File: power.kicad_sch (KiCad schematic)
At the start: 60 parts, among them J19 Conn_Coaxial, Q1 CSD18511Q5A, Q2 CSD18511Q5A, Q3 CSD18511Q5A, Q4 CSD18511Q5A, U1 LM25119PSQ/NOPB, U2 DS4432U+, U3 INA260

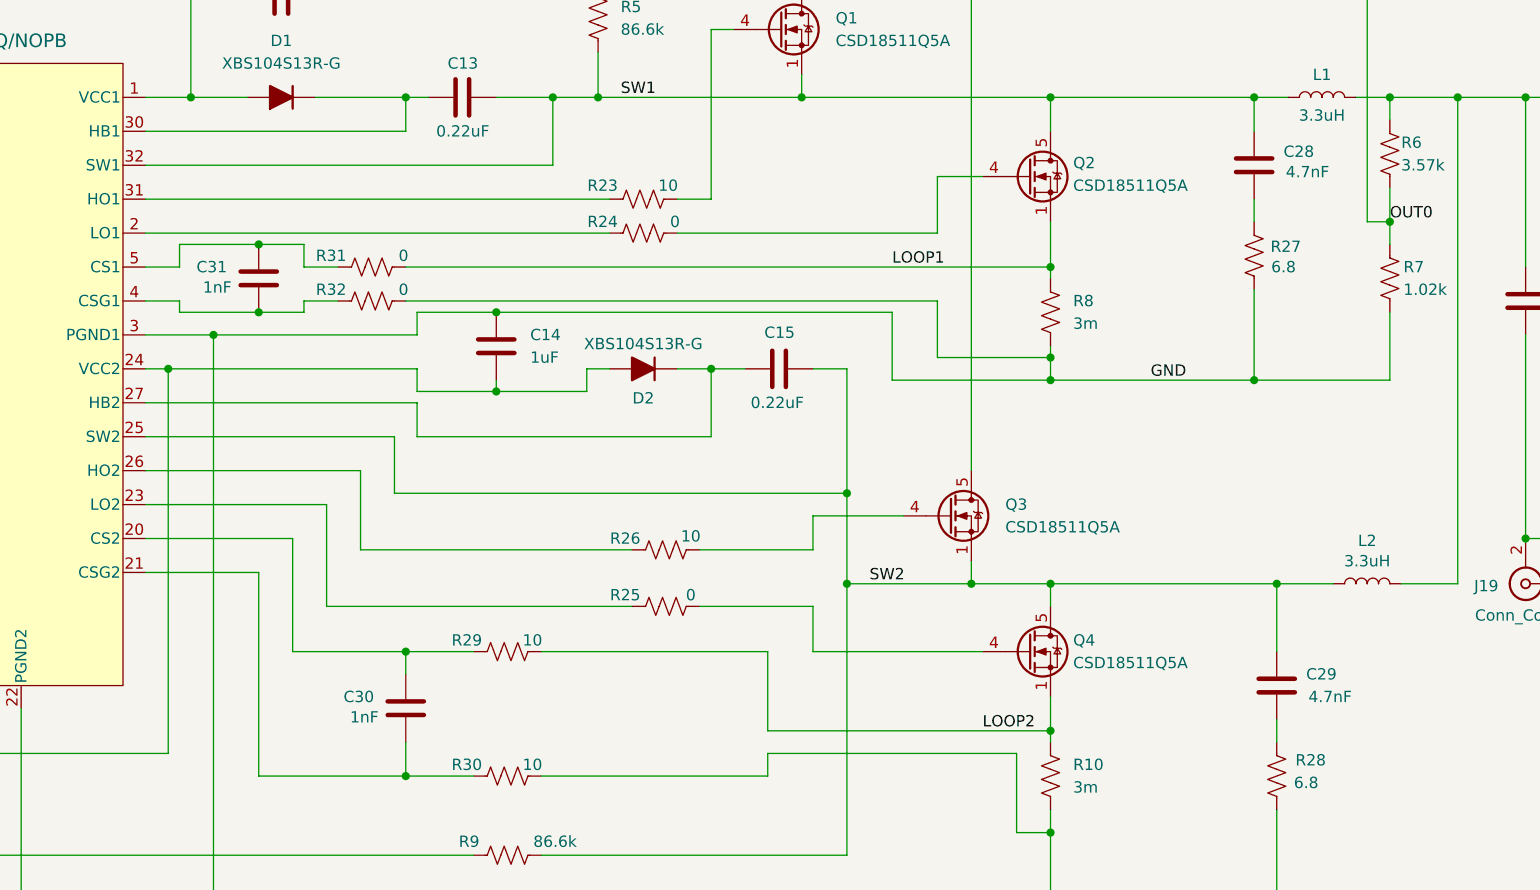
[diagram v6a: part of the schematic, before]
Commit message: reduced center pad paste amount. cleaned up ASIC footprint vias. moved vreg passives around to better fit model name
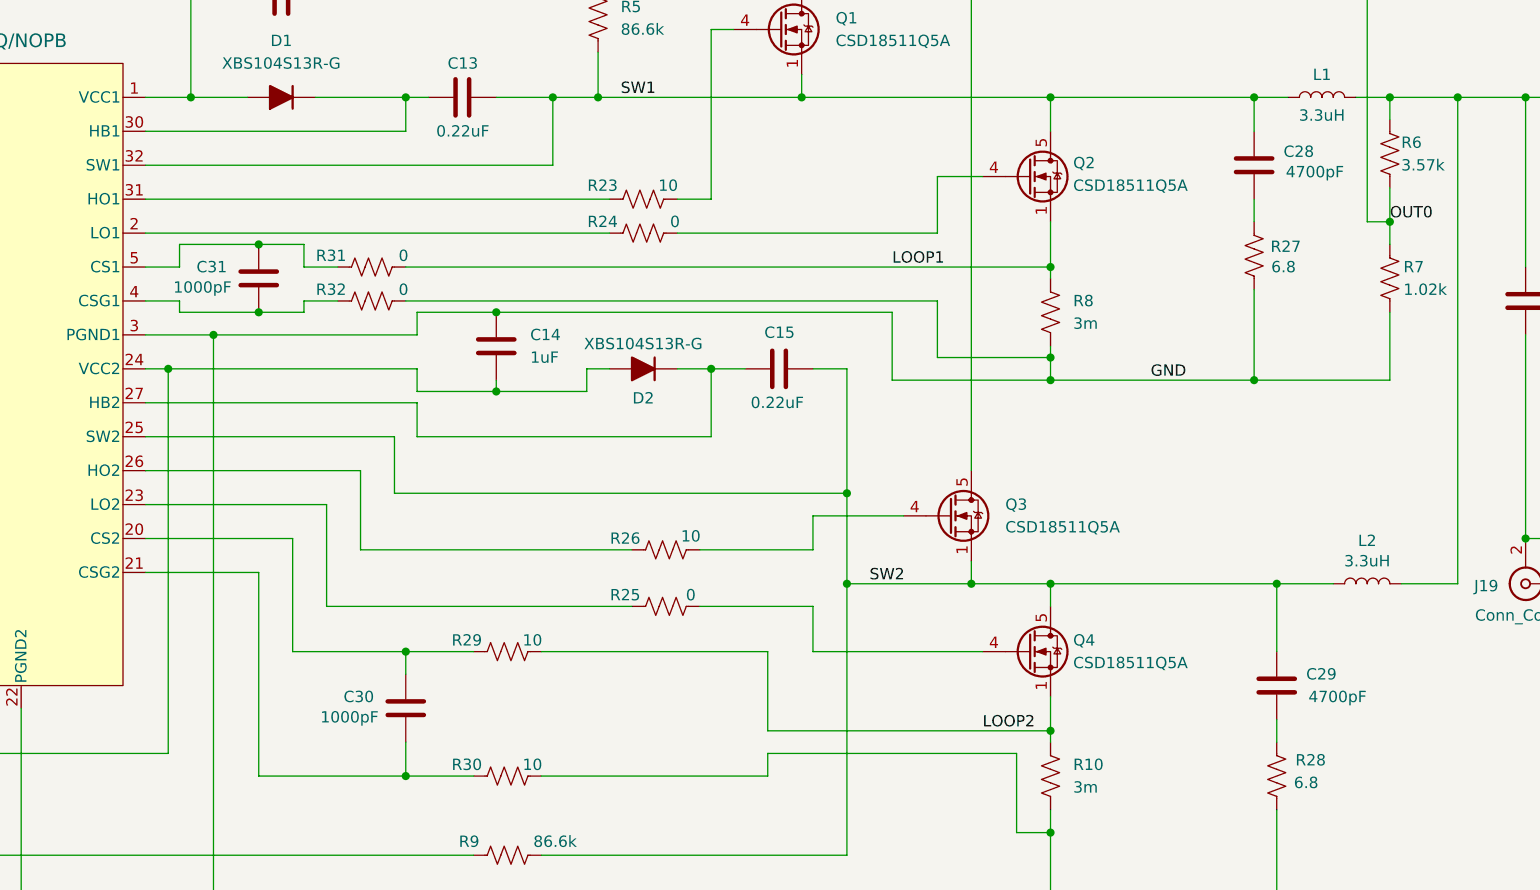
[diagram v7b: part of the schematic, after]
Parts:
- C26: DK (none) -> 1276-6470-1-ND; PARTNO (none) -> CL21B105KBFNNNG
- C27: DK (none) -> 311-1140-1-ND; PARTNO (none) -> CC0805KRX7R9BB104
- C28, C29: value 4.7nF -> 4700pF; DK (none) -> 311-1133-1-ND; PARTNO (none) -> CC0805KRX7R9BB472
- C30, C31: value 1nF -> 1000pF; DK (none) -> 1276-1169-1-ND; PARTNO (none) -> CL21B102KCANNNC
- R11: DK (none) -> 311-39.0KLRCT-ND; PARTNO (none) -> RC0402FR-0739KL
- R23, R26, R29, R30: DK (none) -> 311-10.0HRCT-ND; PARTNO (none) -> RC0603FR-0710RL
- R24, R25, R31, R32, R33: DK (none) -> 311-0.0HRCT-ND; PARTNO (none) -> RC0603FR-070RL
- R27, R28: DK (none) -> 13-RC0603FR-076R8LCT-ND; PARTNO (none) -> RC0603FR-076R8L
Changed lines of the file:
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@@
 			)
 		)
-		(property "DK" ""
+		(property "DK" "311-1140-1-ND"
 			(at 344.17 95.25 0)
 			(effects
@@
 			)
 		)
-		(property "PARTNO" ""
+		(property "PARTNO" "CC0805KRX7R9BB104"
 			(at 344.17 95.25 0)
 			(effects
@@
 			)
 		)
+		(property "DK" "311-10.0HRCT-ND"
+			(at 229.87 134.62 0)
+			(effects
+				(font
+					(size 1.27 1.27)
+				)
+				(hide yes)
+			)
+		)
+		(property "PARTNO" "RC0603FR-0710RL"
+			(at 229.87 134.62 0)
+			(effects
+				(font
+					(size 1.27 1.27)
+				)
+				(hide yes)
+			)
+		)
 		(pin "1"
 		)
@@
 			)
 		)
+		(property "DK" "311-0.0HRCT-ND"
+			(at 214.63 91.44 0)
+			(effects
+				(font
+					(size 1.27 1.27)
+				)
+				(hide yes)
+			)
+		)
+		(property "PARTNO" "RC0603FR-070RL"
+			(at 214.63 91.44 0)
+			(effects
+				(font
+					(size 1.27 1.27)
+				)
+				(hide yes)
+			)
+		)
 		(pin "1"
 		)
@@
 			)
 		)
-		(property "DK" ""
+		(property "DK" "13-RC0603FR-076R8LCT-ND"
 			(at 316.23 148.59 0)
 			(effects
@@
 			)
 		)
-		(property "PARTNO" ""
+		(property "PARTNO" "RC0603FR-076R8L"
 			(at 316.23 148.59 0)
 			(effects
@@
 			)
 		)
+		(property "DK" "311-10.0HRCT-ND"
+			(at 245.11 83.82 0)
+			(effects
+				(font
+					(size 1.27 1.27)
+				)
+				(hide yes)
+			)
+		)
+		(property "PARTNO" "RC0603FR-0710RL"
+			(at 245.11 83.82 0)
+			(effects
+				(font
+					(size 1.27 1.27)
+				)
+				(hide yes)
+			)
+		)
 		(pin "1"
 		)
@@
 			)
 		)
-		(property "Value" "4.7nF"
+		(property "Value" "4700pF"
 			(at 317.246 80.772 0)
 			(effects
@@
 			)
 		)
-		(property "DK" ""
+		(property "DK" "311-1133-1-ND"
 			(at 313.69 80.01 0)
 			(effects
@@
 			)
 		)
-		(property "PARTNO" ""
+		(property "PARTNO" "CC0805KRX7R9BB472"
 			(at 313.69 80.01 0)
 			(effects
@@
 			)
 		)
+		(property "DK" "311-10.0HRCT-ND"
+			(at 247.65 123.19 0)
+			(effects
+				(font
+					(size 1.27 1.27)
+				)
+				(hide yes)
+			)
+		)
+		(property "PARTNO" "RC0603FR-0710RL"
+			(at 247.65 123.19 0)
+			(effects
+				(font
+					(size 1.27 1.27)
+				)
+				(hide yes)
+			)
+		)
 		(pin "1"
 		)
@@
 			)
 		)
-		(property "DK" ""
+		(property "DK" "13-RC0603FR-076R8LCT-ND"
 			(at 313.69 90.17 0)
 			(effects
@@
 			)
 		)
-		(property "PARTNO" ""
+		(property "PARTNO" "RC0603FR-076R8L"
 			(at 313.69 90.17 0)
 			(effects
@@
 			)
 		)
+		(property "DK" "311-0.0HRCT-ND"
+			(at 247.65 129.54 0)
+			(effects
+				(font
+					(size 1.27 1.27)
+				)
+				(hide yes)
+			)
+		)
+		(property "PARTNO" "RC0603FR-070RL"
+			(at 247.65 129.54 0)
+			(effects
+				(font
+					(size 1.27 1.27)
+				)
+				(hide yes)
+			)
+		)
 		(pin "1"
 		)
@@
 			)
 		)
+		(property "DK" "311-0.0HRCT-ND"
+			(at 214.63 95.25 0)
+			(effects
+				(font
+					(size 1.27 1.27)
+				)
+				(hide yes)
+			)
+		)
+		(property "PARTNO" "RC0603FR-070RL"
+			(at 214.63 95.25 0)
+			(effects
+				(font
+					(size 1.27 1.27)
+				)
+				(hide yes)
+			)
+		)
 		(pin "1"
 		)
@@
 			)
 		)
-		(property "Value" "1nF"
+		(property "Value" "1000pF"
 			(at 215.392 141.986 0)
 			(effects
@@
 			)
 		)
-		(property "DK" ""
+		(property "DK" "1276-1169-1-ND"
 			(at 218.44 140.97 0)
 			(effects
@@
 			)
 		)
-		(property "PARTNO" ""
+		(property "PARTNO" "CL21B102KCANNNC"
 			(at 218.44 140.97 0)
 			(effects
@@
 			)
 		)
+		(property "DK" "311-0.0HRCT-ND"
+			(at 245.11 87.63 0)
+			(effects
+				(font
+					(size 1.27 1.27)
+				)
+				(hide yes)
+			)
+		)
+		(property "PARTNO" "RC0603FR-070RL"
+			(at 245.11 87.63 0)
+			(effects
+				(font
+					(size 1.27 1.27)
+				)
+				(hide yes)
+			)
+		)
 		(pin "1"
 		)
@@
 			)
 		)
-		(property "Value" "1nF"
+		(property "Value" "1000pF"
 			(at 198.882 93.726 0)
 			(effects
@@
 			)
 		)
-		(property "DK" ""
+		(property "DK" "1276-1169-1-ND"
 			(at 201.93 92.71 0)
 			(effects
@@
 			)
 		)
-		(property "PARTNO" ""
+		(property "PARTNO" "CL21B102KCANNNC"
 			(at 201.93 92.71 0)
 			(effects
@@
 			)
 		)
+		(property "DK" "311-10.0HRCT-ND"
+			(at 229.87 148.59 0)
+			(effects
+				(font
+					(size 1.27 1.27)
+				)
+				(hide yes)
+			)
+		)
+		(property "PARTNO" "RC0603FR-0710RL"
+			(at 229.87 148.59 0)
+			(effects
+				(font
+					(size 1.27 1.27)
+				)
+				(hide yes)
+			)
+		)
 		(pin "1"
 		)
@@
 			)
 		)
-		(property "Value" "4.7nF"
+		(property "Value" "4700pF"
 			(at 319.786 139.7 0)
 			(effects
@@
 			)
 		)
-		(property "DK" ""
+		(property "DK" "311-1133-1-ND"
 			(at 316.23 138.43 0)
 			(effects
@@
 			)
 		)
-		(property "PARTNO" ""
+		(property "PARTNO" "CC0805KRX7R9BB472"
 			(at 316.23 138.43 0)
 			(effects
@@
 			)
 		)
+		(property "DK" "311-0.0HRCT-ND"
+			(at 77.47 78.74 0)
+			(effects
+				(font
+					(size 1.27 1.27)
+				)
+				(hide yes)
+			)
+		)
+		(property "PARTNO" "RC0603FR-070RL"
+			(at 77.47 78.74 0)
+			(effects
+				(font
+					(size 1.27 1.27)
+				)
+				(hide yes)
+			)
+		)
 		(pin "1"
 		)
@@
 			)
 		)
-		(property "DK" ""
+		(property "DK" "1276-6470-1-ND"
 			(at 355.6 95.25 0)
 			(effects
@@
 			)
 		)
-		(property "PARTNO" ""
+		(property "PARTNO" "CL21B105KBFNNNG"
 			(at 355.6 95.25 0)
 			(effects
@@
 			)
 		)
-		(property "DK" ""
+		(property "DK" "311-39.0KLRCT-ND"
 			(at 295.91 219.71 0)
 			(effects
@@
 			)
 		)
-		(property "PARTNO" ""
+		(property "PARTNO" "RC0402FR-0739KL"
 			(at 295.91 219.71 0)
 			(effects

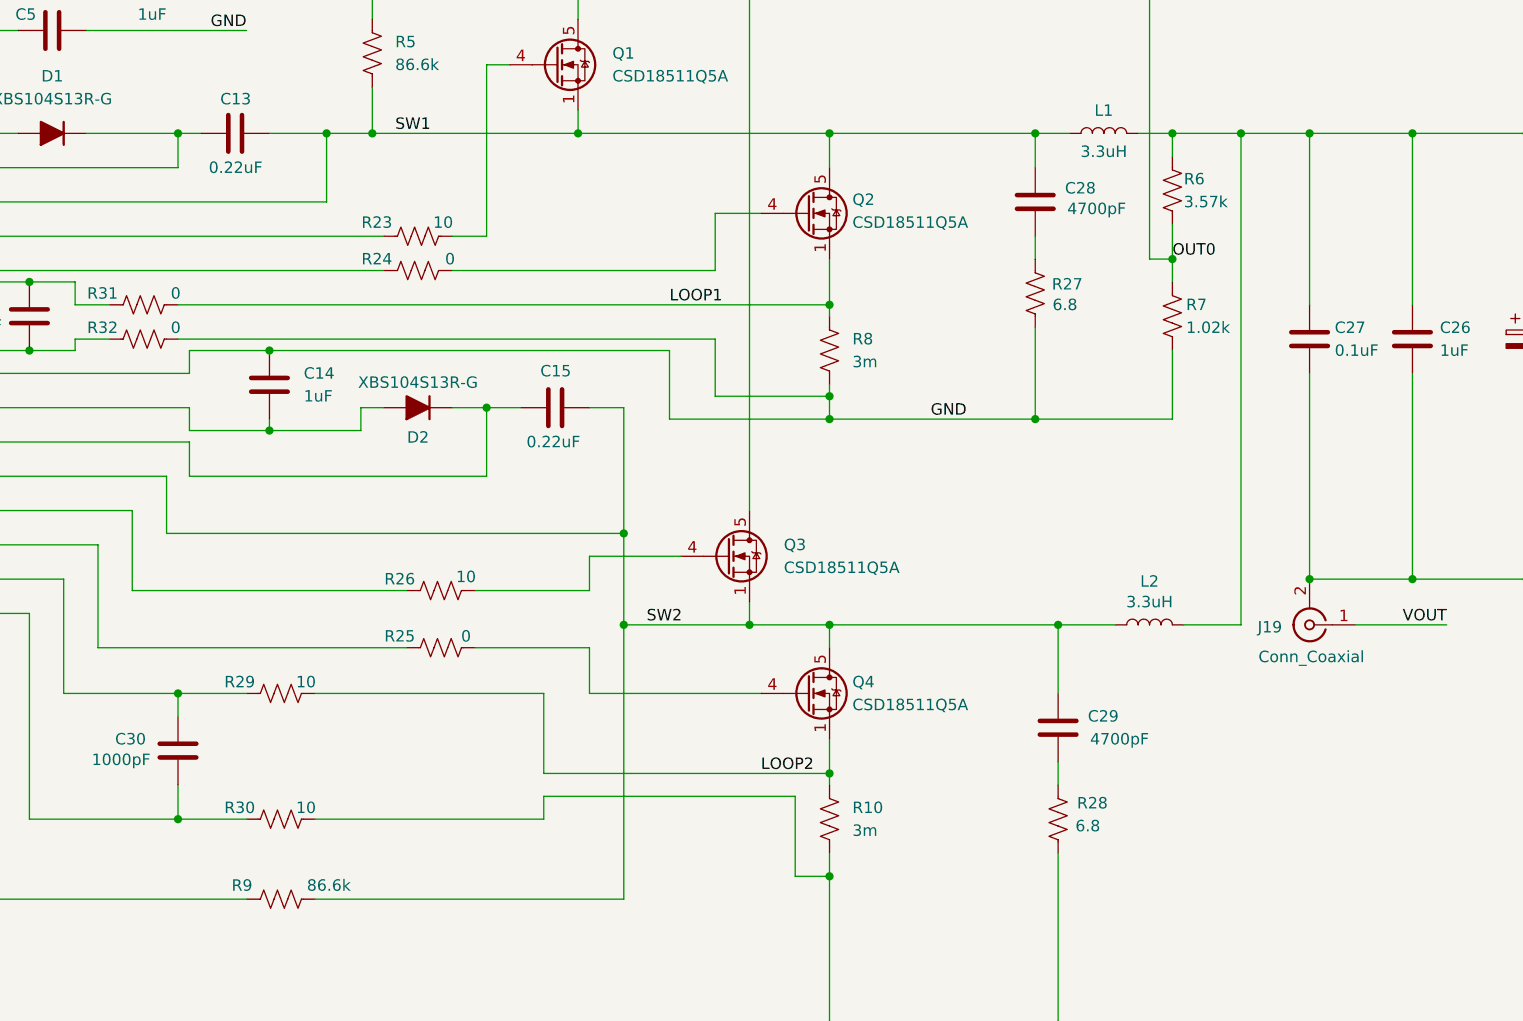
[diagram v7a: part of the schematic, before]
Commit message: DNP low side FET snubber circuit for now (to be redone in v4). Update current sense resistor filter values. regenerate BOM, iBOM. Slight slikscreen cleanup. regenerated gerbers
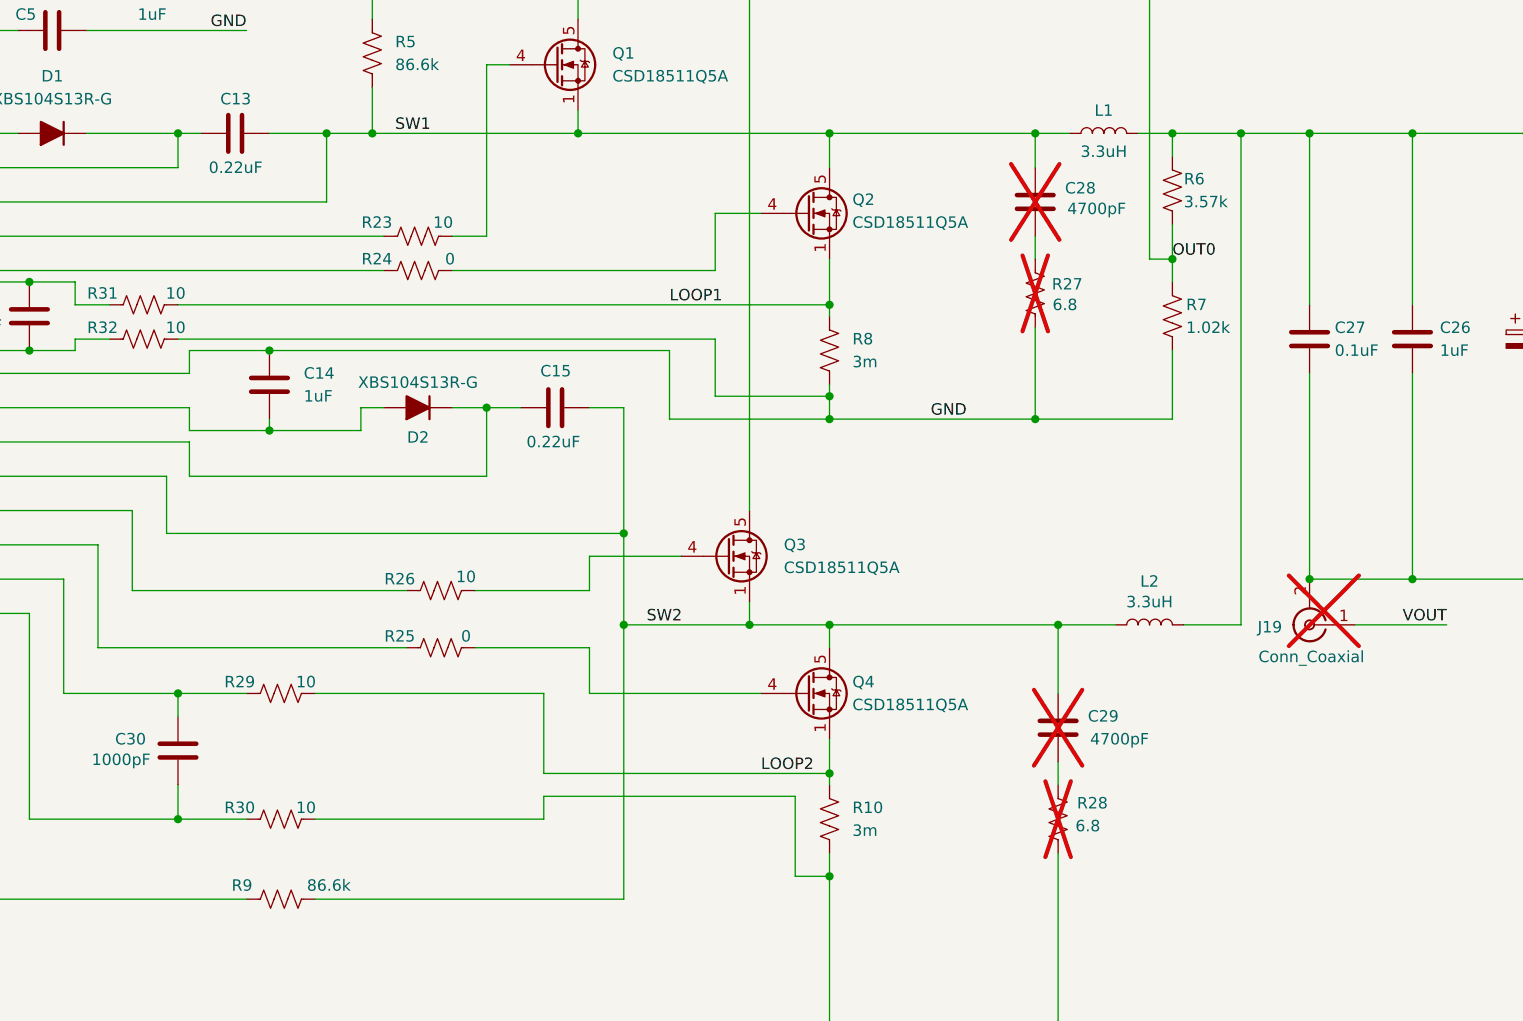
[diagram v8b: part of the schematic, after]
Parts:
- C28, C29, J19, R27, R28: now not fitted; now left out of the parts list
- R31, R32: value 0 -> 10; DK 311-0.0HRCT-ND -> 311-10.0HRCT-ND; PARTNO RC0603FR-070RL -> RC0603FR-0710RL
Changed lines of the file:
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@@
 			)
 		)
-		(property "Value" "0"
+		(property "Value" "10"
 			(at 218.186 90.17 90)
 			(effects
@@
 			)
 		)
-		(property "DK" "311-0.0HRCT-ND"
+		(property "DK" "311-10.0HRCT-ND"
 			(at 214.63 91.44 0)
 			(effects
@@
 			)
 		)
-		(property "PARTNO" "RC0603FR-070RL"
+		(property "PARTNO" "RC0603FR-0710RL"
 			(at 214.63 91.44 0)
 			(effects
@@
 		(unit 1)
 		(exclude_from_sim no)
-		(in_bom yes)
+		(in_bom no)
 		(on_board yes)
-		(dnp no)
+		(dnp yes)
 		(property "Reference" "R28"
 			(at 320.04 146.812 0)
@@
 		(unit 1)
 		(exclude_from_sim no)
-		(in_bom yes)
+		(in_bom no)
 		(on_board yes)
-		(dnp no)
+		(dnp yes)
 		(property "Reference" "C28"
 			(at 316.992 78.486 0)
@@
 		(unit 1)
 		(exclude_from_sim no)
-		(in_bom yes)
+		(in_bom no)
 		(on_board yes)
-		(dnp no)
+		(dnp yes)
 		(property "Reference" "R27"
 			(at 317.246 89.154 0)
@@
 		(unit 1)
 		(exclude_from_sim no)
-		(in_bom yes)
+		(in_bom no)
 		(on_board yes)
-		(dnp no)
+		(dnp yes)
 		(property "Reference" "J19"
 			(at 341.122 127.254 0)
@@
 			)
 		)
-		(property "Value" "0"
+		(property "Value" "10"
 			(at 218.186 93.98 90)
 			(effects
@@
 			)
 		)
-		(property "DK" "311-0.0HRCT-ND"
+		(property "DK" "311-10.0HRCT-ND"
 			(at 214.63 95.25 0)
 			(effects
@@
 			)
 		)
-		(property "PARTNO" "RC0603FR-070RL"
+		(property "PARTNO" "RC0603FR-0710RL"
 			(at 214.63 95.25 0)
 			(effects
@@
 		(unit 1)
 		(exclude_from_sim no)
-		(in_bom yes)
+		(in_bom no)
 		(on_board yes)
-		(dnp no)
+		(dnp yes)
 		(property "Reference" "C29"
 			(at 319.532 137.16 0)
